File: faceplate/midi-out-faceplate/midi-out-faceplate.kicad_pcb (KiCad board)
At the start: 2 copper layers, 98 x 30 mm, 0 parts

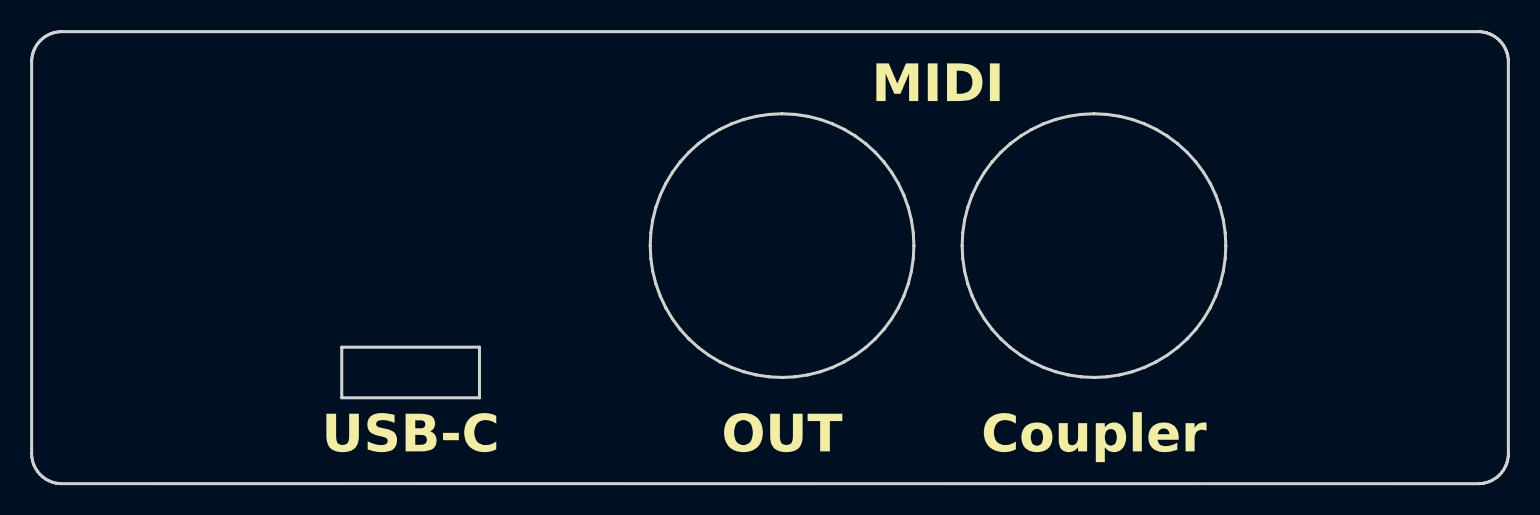
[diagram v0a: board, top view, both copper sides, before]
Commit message: Update faceplates by moving all the holes up 1.6mm
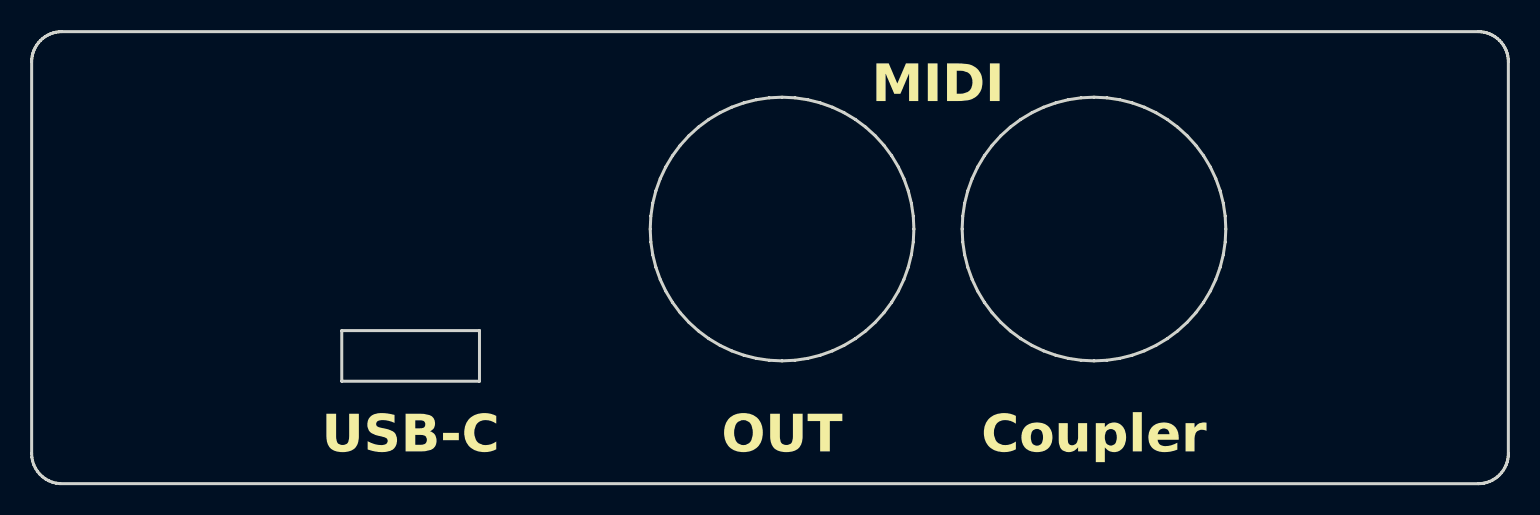
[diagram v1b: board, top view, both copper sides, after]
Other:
- outline, holes or cut-outs redrawn
- board text added: "v2.1.0"
- board text removed: "v2.1.0b1"

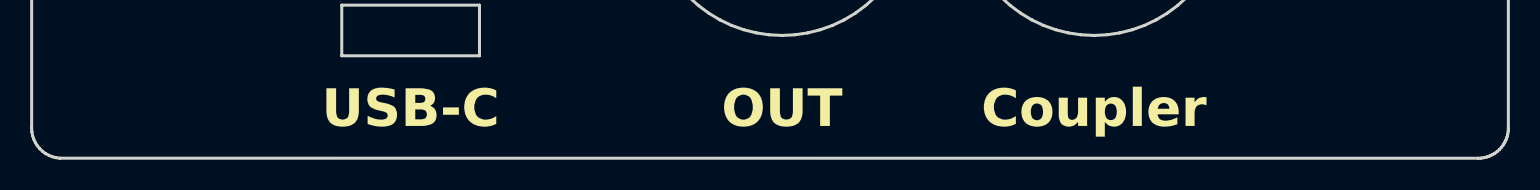
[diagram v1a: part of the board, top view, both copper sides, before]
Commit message: Update offset around JST connector to 0.2mm (from 0.1mm)
Update version numbers to 3.0.0
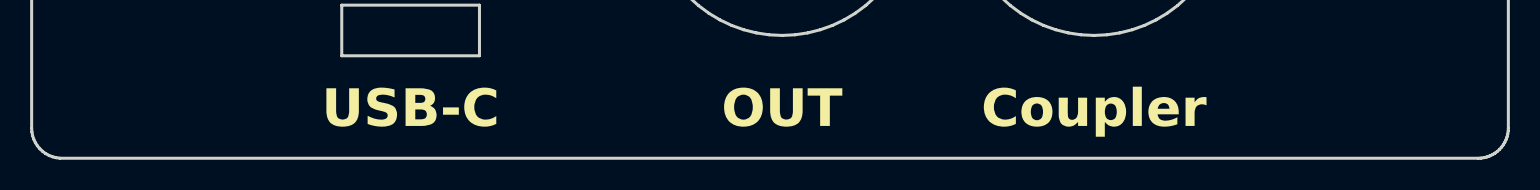
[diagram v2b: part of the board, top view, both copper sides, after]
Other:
- board text added: "v3.0.0"
- board text removed: "v2.1.0"
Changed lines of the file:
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@@
   (title_block
     (title "MIDI OUT Faceplate")
-    (date "2023-03-15")
-    (rev "2.1.0")
+    (date "2023-07-03")
+    (rev "3.0.0")
     (company "Dave Dribin")
   )
@@
   (gr_line (start 163.7361 87.5491) (end 164.3128 86.9128)
     (stroke (width 0.2) (type solid)) (layer "Edge.Cuts"))
-  (gr_line (start 101.8744 109.996063) (end 196 110)
+  (gr_line (start 101.8744 110) (end 196 110)
     (stroke (width 0.2) (type solid)) (layer "Edge.Cuts"))
   (gr_line (start 172.207 84.5181) (end 173.04 84.7268)
@@
   (gr_line (start 196.9428 80.2362) (end 196.7654 80.1523)
     (stroke (width 0.2) (type solid)) (layer "Edge.Cuts"))
-  (gr_text "v2.1.0" (at 195 109) (layer "B.SilkS")
+  (gr_text "v3.0.0" (at 195 109) (layer "B.SilkS")
     (effects (font (size 1 1) (thickness 0.15)) (justify left bottom mirror))
   )
